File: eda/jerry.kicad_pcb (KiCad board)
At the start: 2 copper layers, 57.8 x 39.4 mm, 32 parts, among them J1 Conn_01x06_Socket, U1 NE555P, U10 74LS08, U2 74LS393, U3 74HC595, U4 74LS266, U5 74HC74, U6 74HC04, U7 74LS21, U8 NE555P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

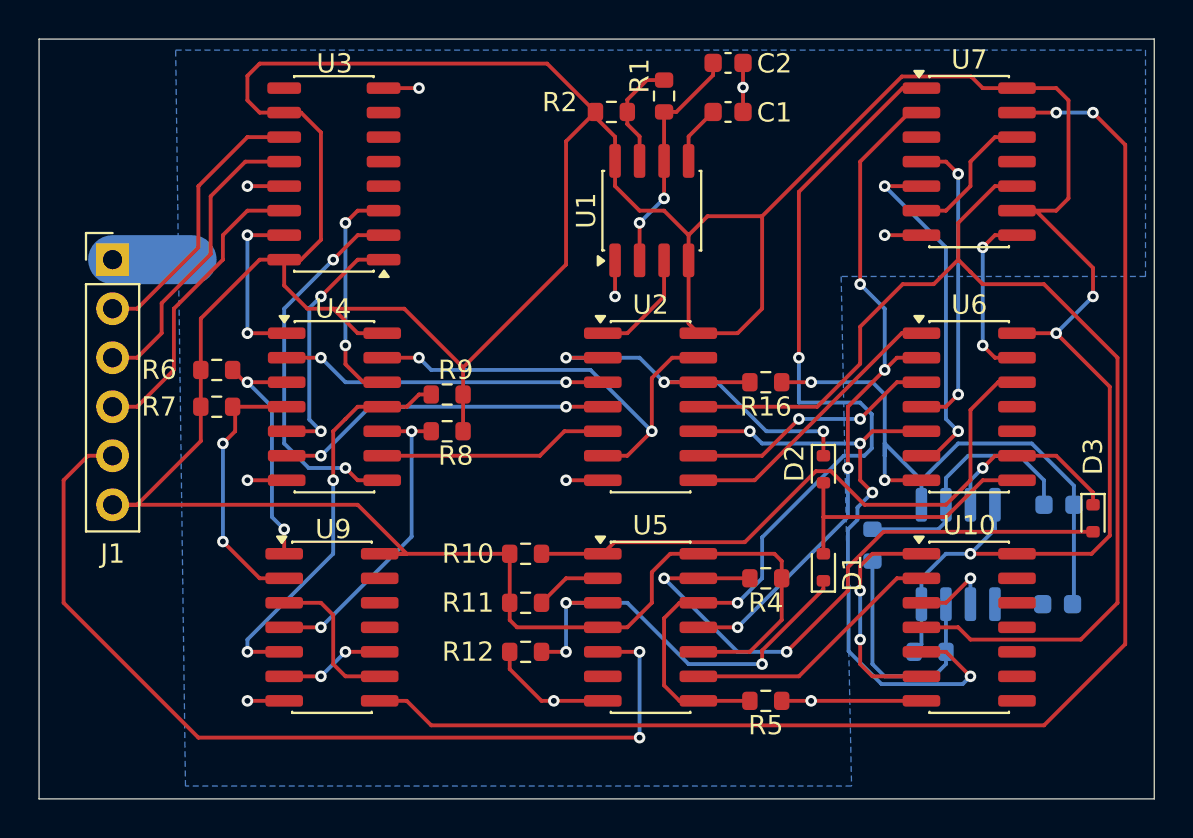
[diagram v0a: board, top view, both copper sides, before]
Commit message: Reorganized repository
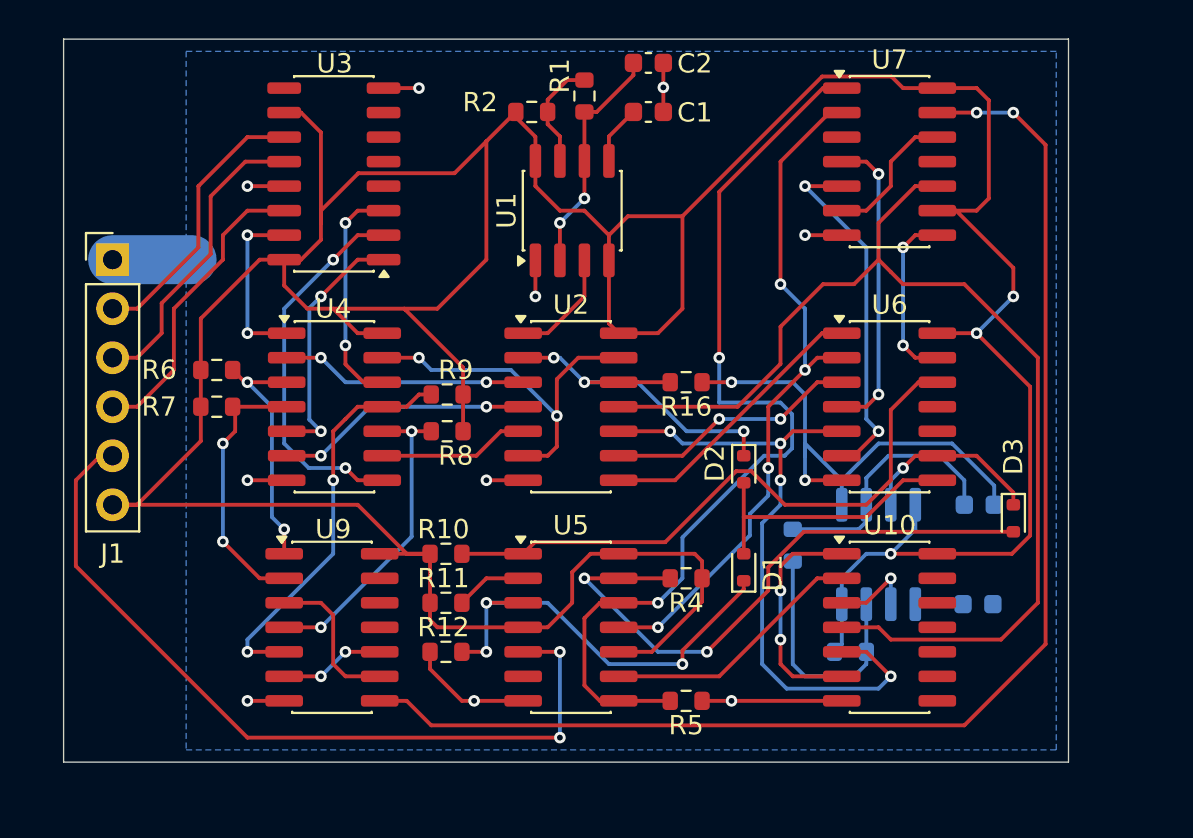
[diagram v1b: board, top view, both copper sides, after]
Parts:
- moved D1 4.13 mm to (128.0, 103.6)
- moved D2 4.13 mm to (128.0, 98.5)
- moved R10 4.13 mm to (112.5, 102.9)
- moved R11 4.13 mm to (112.5, 105.4)
- moved R12 4.13 mm to (112.5, 108.0)
- moved C1 4.13 mm to (123.0, 80.0)
- moved C2 4.13 mm to (123.0, 77.4)
- moved C3 4.13 mm to (140.1, 105.5)
- moved C4 4.13 mm to (140.2, 100.3)
- moved D3 4.13 mm to (141.9, 101.0)
- moved R1 4.13 mm to (119.7, 79.2)
- moved R13 4.13 mm to (130.5, 102.4)
- moved R15 4.13 mm to (133.5, 108.0)
- moved R16 4.13 mm to (125.0, 94.0)
- moved R2 4.13 mm to (117.0, 80.0)
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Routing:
- net VCC: track 233.8 -> 214.4 mm
- net OUT: track 48.5 -> 42.0 mm
- net GND: track 65.9 -> 60.8 mm
- net Net-(U2A-Q3): track 24.2 -> 19.6 mm
- net Net-(U2A-Q1): track 17.4 -> 13.3 mm
- net Net-(U2A-Q0): track 16.9 -> 12.8 mm
- net Net-(U2A-Q2): track 12.0 -> 7.83 mm
- net Net-(U7-Pad13): track 73.1 -> 68.9 mm
- net /MS_CNTR_RST: track 22.5 -> 18.7 mm
- net Net-(U2B-Q1): track 34.5 -> 35.1 mm
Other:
- board size 57.8 x 39.4 mm -> 52.1 x 37.5 mm
